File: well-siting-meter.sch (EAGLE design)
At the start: 46 parts, among them J2 7805, T1 MOSFET-NCHANNELFQP30N06L, U1 LCD-16X2NOHOLES, U2 ARDUINO_PRO_MINI, U3 EC2, U4 EC2, U5 AD623, U6 AD623

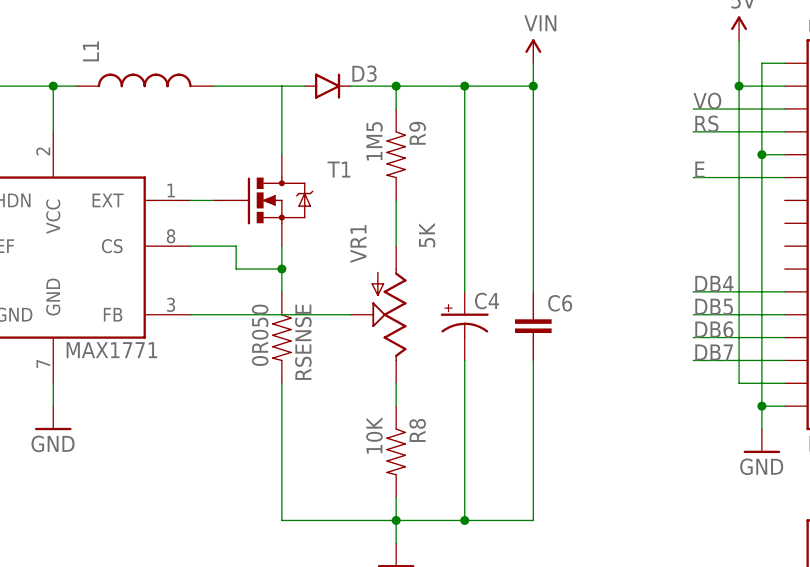
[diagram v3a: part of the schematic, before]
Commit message: adding part numbers
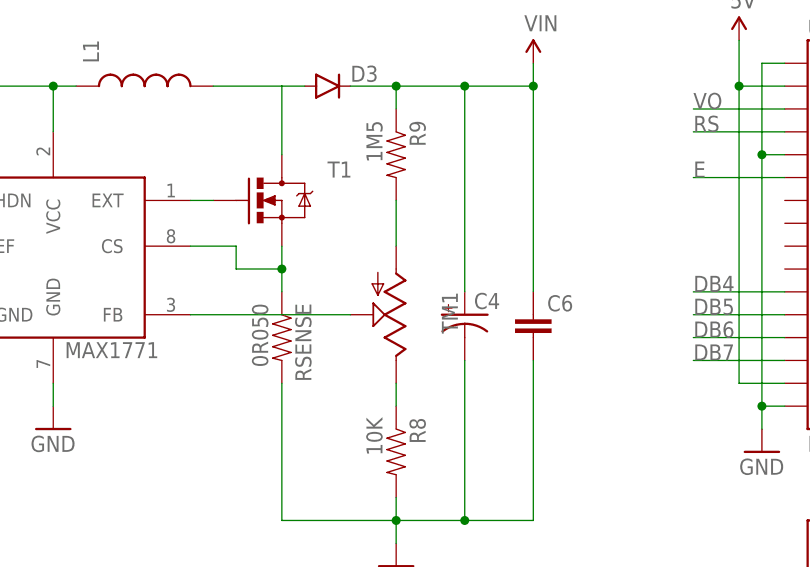
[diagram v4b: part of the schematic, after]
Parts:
- removed VR1: 5K, SparkFun-Electromechanical:POTTRIM
- added TM1: (no value), adafruit:TRIM3386
- D3: PN (none) -> EGP20FCT-ND
- T1: PN (none) -> FDP33N25-ND
- U$1: PN (none) -> MAX1771CPA+-ND
- U1: PN (none) -> 1528-1502-ND
- U2: PN (none) -> 1568-1055-ND
- U3, U4: PN (none) -> 399-11029-5-ND
- U5, U6: PN (none) -> AD623ANZ-ND
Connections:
- net N$15: now also TM1.S; no longer VR1.S
- net N$6: now also TM1.A; no longer VR1.A
- net N$8: now also TM1.E; no longer VR1.E
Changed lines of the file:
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@@
 <layer number="230" name="230bmp" color="7" fill="1" visible="yes" active="yes"/>
 <layer number="231" name="231bmp" color="7" fill="1" visible="yes" active="yes"/>
+<layer number="232" name="Eagle3D_PG2" color="7" fill="1" visible="no" active="no"/>
+<layer number="233" name="Eagle3D_PG3" color="7" fill="1" visible="no" active="no"/>
 <layer number="248" name="Housing" color="7" fill="1" visible="yes" active="yes"/>
 <layer number="249" name="Edge" color="7" fill="1" visible="yes" active="yes"/>
@@
 </classes>
 <parts>
-<part name="U3" library="ec2" deviceset="EC2" device=""/>
-<part name="U4" library="ec2" deviceset="EC2" device=""/>
-<part name="U2" library="SparkFun-Boards" deviceset="ARDUINO_PRO_MINI" device=""/>
-<part name="U5" library="ad623" deviceset="AD623" device=""/>
-<part name="U6" library="ad623" deviceset="AD623" device=""/>
+<part name="U3" library="ec2" deviceset="EC2" device="">
+<attribute name="PN" value="399-11029-5-ND"/>
+</part>
+<part name="U4" library="ec2" deviceset="EC2" device="">
+<attribute name="PN" value="399-11029-5-ND"/>
+</part>
+<part name="U2" library="SparkFun-Boards" deviceset="ARDUINO_PRO_MINI" device="">
+<attribute name="PN" value="1568-1055-ND"/>
+</part>
+<part name="U5" library="ad623" deviceset="AD623" device="">
+<attribute name="PN" value="AD623ANZ-ND"/>
+</part>
+<part name="U6" library="ad623" deviceset="AD623" device="">
+<attribute name="PN" value="AD623ANZ-ND"/>
+</part>
 <part name="Q1" library="SparkFun-DiscreteSemi" deviceset="TRANSISTOR_NPN" device="P2N2222A"/>
 <part name="Q2" library="SparkFun-DiscreteSemi" deviceset="TRANSISTOR_NPN" device="P2N2222A"/>
@@
 <part name="SUPPLY8" library="SparkFun-Aesthetics" deviceset="V_BATT" device=""/>
 <part name="GND8" library="SparkFun-Aesthetics" deviceset="GND" device=""/>
-<part name="U1" library="SparkFun-Displays" deviceset="LCD-16X2" device="NOHOLES" value="LCD-16X2NOHOLES"/>
+<part name="U1" library="SparkFun-Displays" deviceset="LCD-16X2" device="NOHOLES" value="LCD-16X2NOHOLES">
+<attribute name="PN" value="1528-1502-ND"/>
+</part>
 <part name="GND11" library="SparkFun-Aesthetics" deviceset="GND" device=""/>
 <part name="SUPPLY11" library="SparkFun-Aesthetics" deviceset="5V" device=""/>
@@
 <part name="C2" library="SparkFun-Passives" deviceset="CAP" device="PTH"/>
 <part name="C3" library="SparkFun-Passives" deviceset="CAP" device="PTH"/>
-<part name="T1" library="SparkFun-DiscreteSemi" deviceset="MOSFET-NCHANNEL" device="FQP30N06L"/>
-<part name="D3" library="SparkFun-DiscreteSemi" deviceset="DIODE" device="PTH"/>
+<part name="T1" library="SparkFun-DiscreteSemi" deviceset="MOSFET-NCHANNEL" device="FQP30N06L">
+<attribute name="PN" value="FDP33N25-ND"/>
+</part>
+<part name="D3" library="SparkFun-DiscreteSemi" deviceset="DIODE" device="PTH">
+<attribute name="PN" value="EGP20FCT-ND"/>
+</part>
 <part name="RSENSE" library="SparkFun-Passives" deviceset="RESISTOR" device="PTH-1/4W" value="0R050"/>
-<part name="VR1" library="SparkFun-Electromechanical" deviceset="POT" device="TRIM" value="5K"/>
 <part name="R8" library="SparkFun-Passives" deviceset="RESISTOR" device="PTH-1/4W" value="10K"/>
 <part name="R9" library="SparkFun-Passives" deviceset="RESISTOR" device="PTH-1/4W" value="1M5"/>
@@
 <part name="C4" library="SparkFun-Passives" deviceset="CAP_POL" device="PTH1"/>
 <part name="GND1" library="SparkFun-Aesthetics" deviceset="GND" device=""/>
-<part name="U$1" library="max1771" deviceset="MAX1771" device=""/>
+<part name="U$1" library="max1771" deviceset="MAX1771" device="">
+<attribute name="PN" value="MAX1771CPA+-ND"/>
+</part>
 <part name="R10" library="SparkFun-Passives" deviceset="RESISTOR" device="PTH-1/4W" value="1.02K"/>
 <part name="R11" library="SparkFun-Passives" deviceset="RESISTOR" device="PTH-1/4W" value="1.02K"/>
@@
 <part name="GND14" library="SparkFun-Aesthetics" deviceset="GND" device=""/>
 <part name="GND15" library="SparkFun-Aesthetics" deviceset="GND" device=""/>
+<part name="TM1" library="adafruit" deviceset="TRIM" device="3386"/>
 </parts>
 <sheets>
@@
 </plain>
 <instances>
-<instance part="U3" gate="G$1" x="124.46" y="154.94"/>
-<instance part="U4" gate="G$1" x="193.04" y="154.94"/>
-<instance part="U2" gate="G$1" x="144.78" y="119.38"/>
-<instance part="U5" gate="G$1" x="198.12" y="121.92"/>
-<instance part="U6" gate="G$1" x="198.12" y="81.28"/>
+<instance part="U3" gate="G$1" x="124.46" y="154.94">
+<attribute name="PN" x="124.46" y="154.94" size="1.778" layer="96" display="off"/>
+</instance>
+<instance part="U4" gate="G$1" x="193.04" y="154.94">
+<attribute name="PN" x="193.04" y="154.94" size="1.778" layer="96" display="off"/>
+</instance>
+<instance part="U2" gate="G$1" x="144.78" y="119.38">
+<attribute name="PN" x="144.78" y="119.38" size="1.778" layer="96" display="off"/>
+</instance>
+<instance part="U5" gate="G$1" x="198.12" y="121.92">
+<attribute name="PN" x="198.12" y="121.92" size="1.778" layer="96" display="off"/>
+</instance>
+<instance part="U6" gate="G$1" x="198.12" y="81.28">
+<attribute name="PN" x="198.12" y="81.28" size="1.778" layer="96" display="off"/>
+</instance>
 <instance part="Q1" gate="G$1" x="99.06" y="157.48"/>
 <instance part="Q2" gate="G$1" x="167.64" y="157.48"/>
@@
 <instance part="SUPPLY8" gate="G$1" x="25.4" y="86.36"/>
 <instance part="GND8" gate="1" x="25.4" y="48.26"/>
-<instance part="U1" gate="G$1" x="154.94" y="66.04"/>
+<instance part="U1" gate="G$1" x="154.94" y="66.04">
+<attribute name="PN" x="154.94" y="66.04" size="1.778" layer="96" display="off"/>
+</instance>
 <instance part="GND11" gate="1" x="142.24" y="43.18"/>
 <instance part="SUPPLY11" gate="G$1" x="139.7" y="88.9"/>
@@
 <instance part="T1" gate="G$1" x="88.9" y="71.12" smashed="yes">
 <attribute name="NAME" x="93.98" y="73.66" size="1.778" layer="95"/>
-</instance>
-<instance part="D3" gate="G$1" x="93.98" y="83.82"/>
+<attribute name="PN" x="88.9" y="71.12" size="1.778" layer="96" display="off"/>
+</instance>
+<instance part="D3" gate="G$1" x="93.98" y="83.82">
+<attribute name="PN" x="93.98" y="83.82" size="1.778" layer="96" display="off"/>
+</instance>
 <instance part="RSENSE" gate="G$1" x="88.9" y="55.88" rot="R270"/>
-<instance part="VR1" gate="G$1" x="101.6" y="58.42" rot="R180"/>
 <instance part="R8" gate="G$1" x="101.6" y="43.18" rot="R270"/>
 <instance part="R9" gate="G$1" x="101.6" y="76.2" rot="R270"/>
@@
 <instance part="C4" gate="G$1" x="109.22" y="58.42"/>
 <instance part="GND1" gate="1" x="63.5" y="45.72"/>
-<instance part="U$1" gate="G$1" x="63.5" y="63.5"/>
+<instance part="U$1" gate="G$1" x="63.5" y="63.5">
+<attribute name="PN" x="63.5" y="63.5" size="1.778" layer="96" display="off"/>
+</instance>
 <instance part="R10" gate="G$1" x="215.9" y="121.92"/>
 <instance part="R11" gate="G$1" x="215.9" y="81.28"/>
@@
 <instance part="GND14" gate="1" x="223.52" y="106.68"/>
 <instance part="GND15" gate="1" x="223.52" y="66.04"/>
+<instance part="TM1" gate="G$1" x="101.6" y="58.42" rot="R180"/>
 </instances>
 <busses>
@@
 <segment>
 <pinref part="R9" gate="G$1" pin="2"/>
-<pinref part="VR1" gate="G$1" pin="A"/>
 <wire x1="101.6" y1="71.12" x2="101.6" y2="66.04" width="0.1524" layer="91"/>
+<pinref part="TM1" gate="G$1" pin="A"/>
 </segment>
 </net>
 <net name="N$8" class="0">
 <segment>
-<pinref part="VR1" gate="G$1" pin="E"/>
 <pinref part="R8" gate="G$1" pin="1"/>
 <wire x1="101.6" y1="50.8" x2="101.6" y2="48.26" width="0.1524" layer="91"/>
+<pinref part="TM1" gate="G$1" pin="E"/>
 </segment>
 </net>
 <net name="N$15" class="0">
 <segment>
-<pinref part="VR1" gate="G$1" pin="S"/>
 <wire x1="78.74" y1="58.42" x2="96.52" y2="58.42" width="0.1524" layer="91"/>
 <pinref part="U$1" gate="G$1" pin="FB"/>
-</segment>
-</net>
+<pinref part="TM1" gate="G$1" pin="S"/>
+</segment>
+</net>

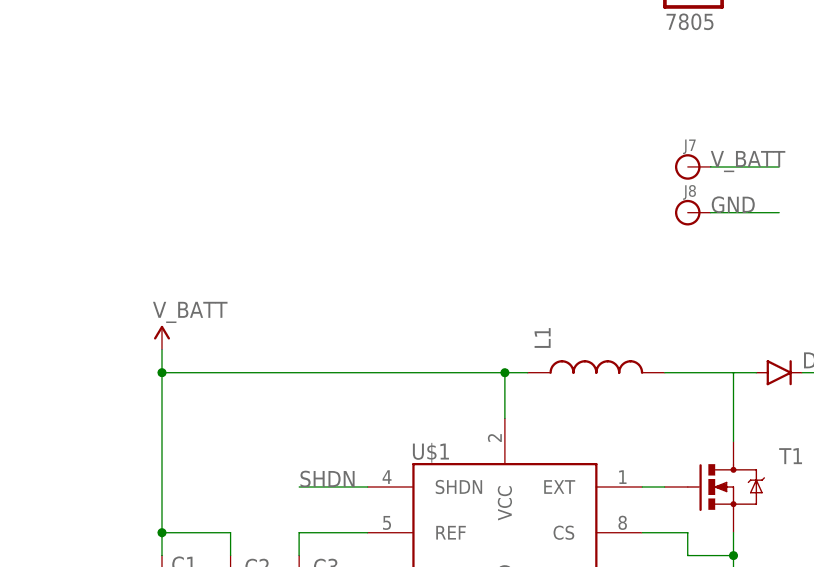
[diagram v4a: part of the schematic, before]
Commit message: updated inductor, adding part numbers
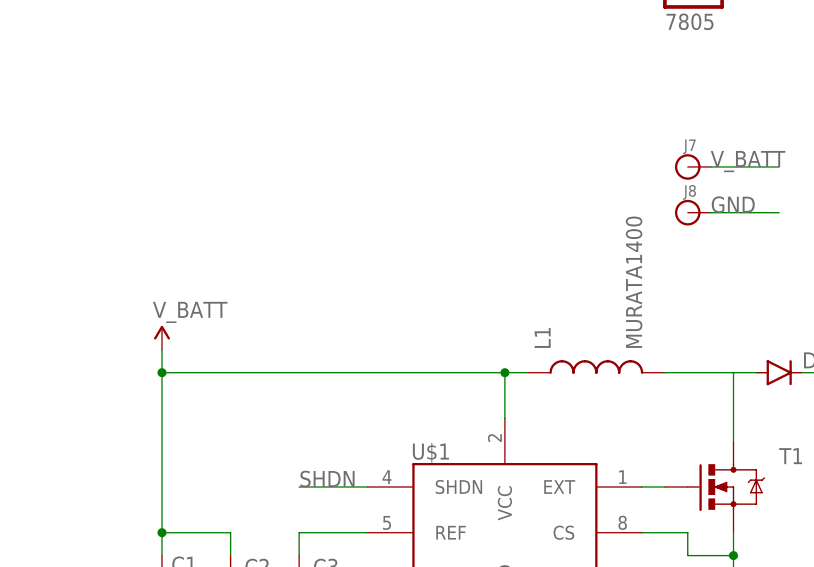
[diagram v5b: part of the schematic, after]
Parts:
- D1, D2: PN (none) -> 1N4001FSCT-ND
- L1: value (none) -> MURATA1400; device SparkFun-Passives:INDUCTORRLB0912 -> murata1400:MURATA1400; PN (none) -> 811-2633-ND
- Q1, Q2: PN (none) -> PN2222AFS-ND
- RSENSE: device SparkFun-Passives:RESISTORPTH-1/4W -> SparkFun-Passives:RESISTORPTH-1W
- S1, S2: PN (none) -> SW406-ND

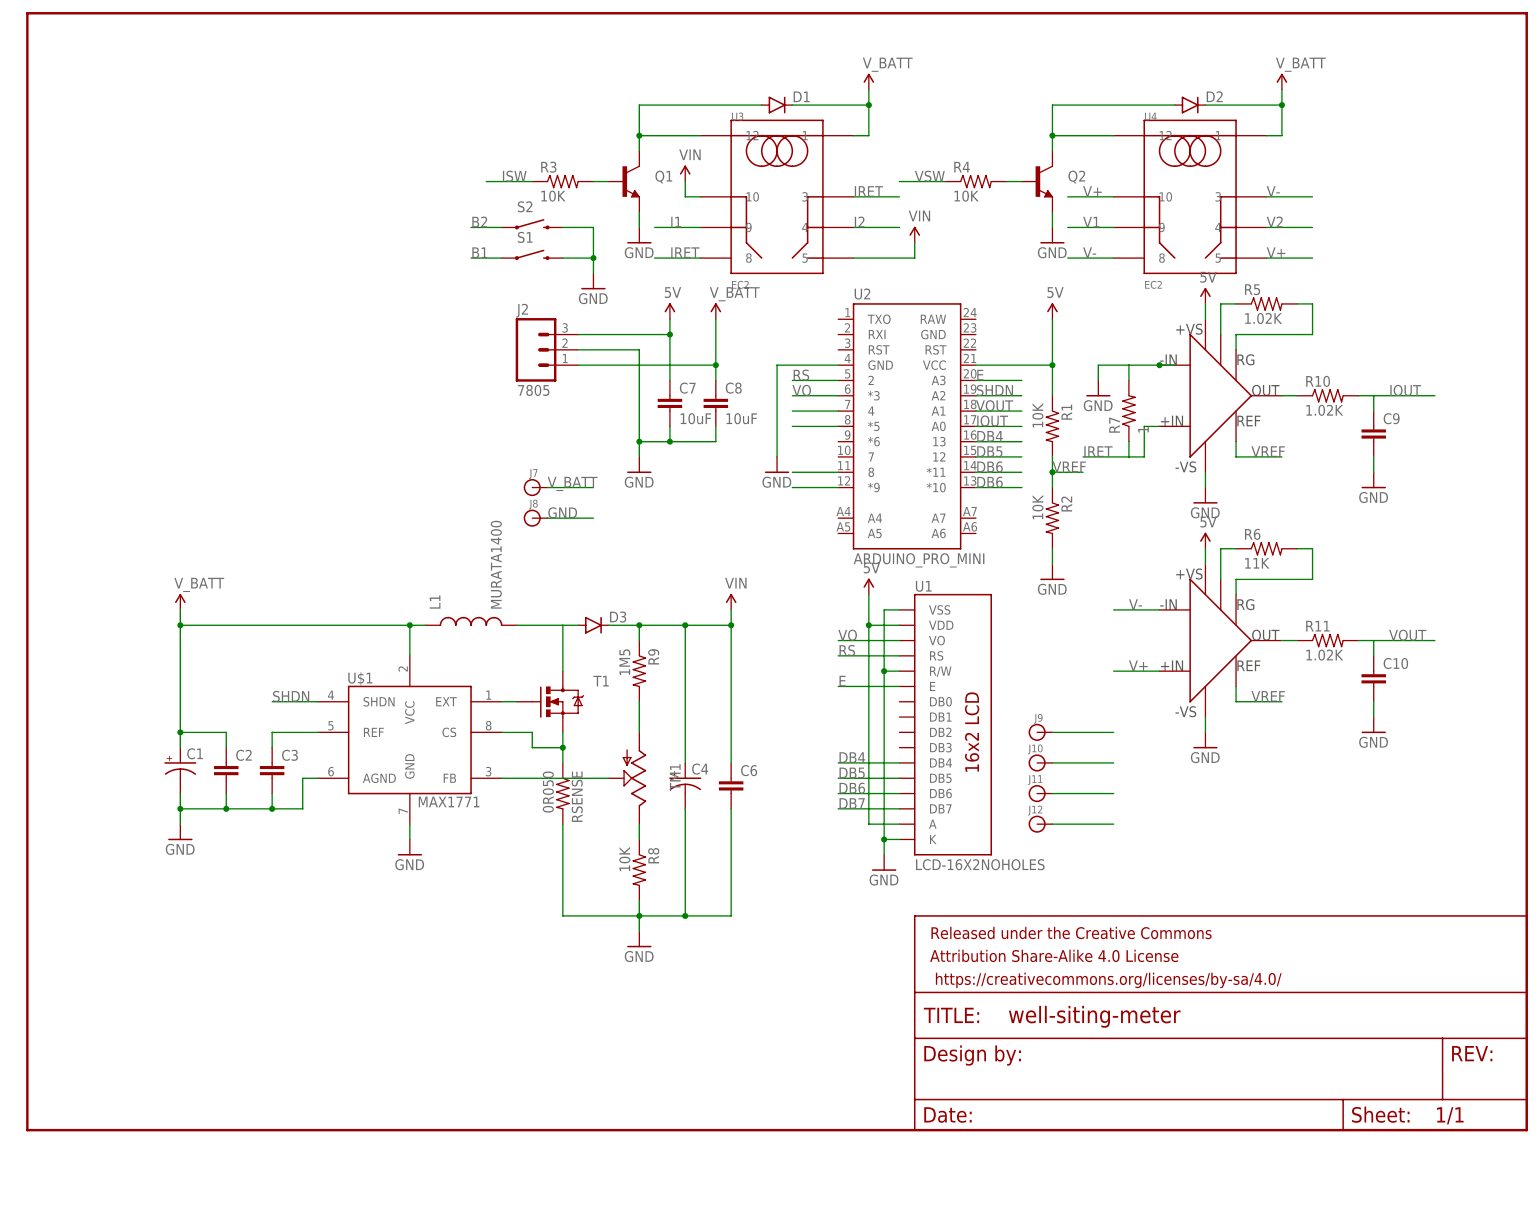
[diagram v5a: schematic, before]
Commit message: fixed board outline, added remaining part numbers
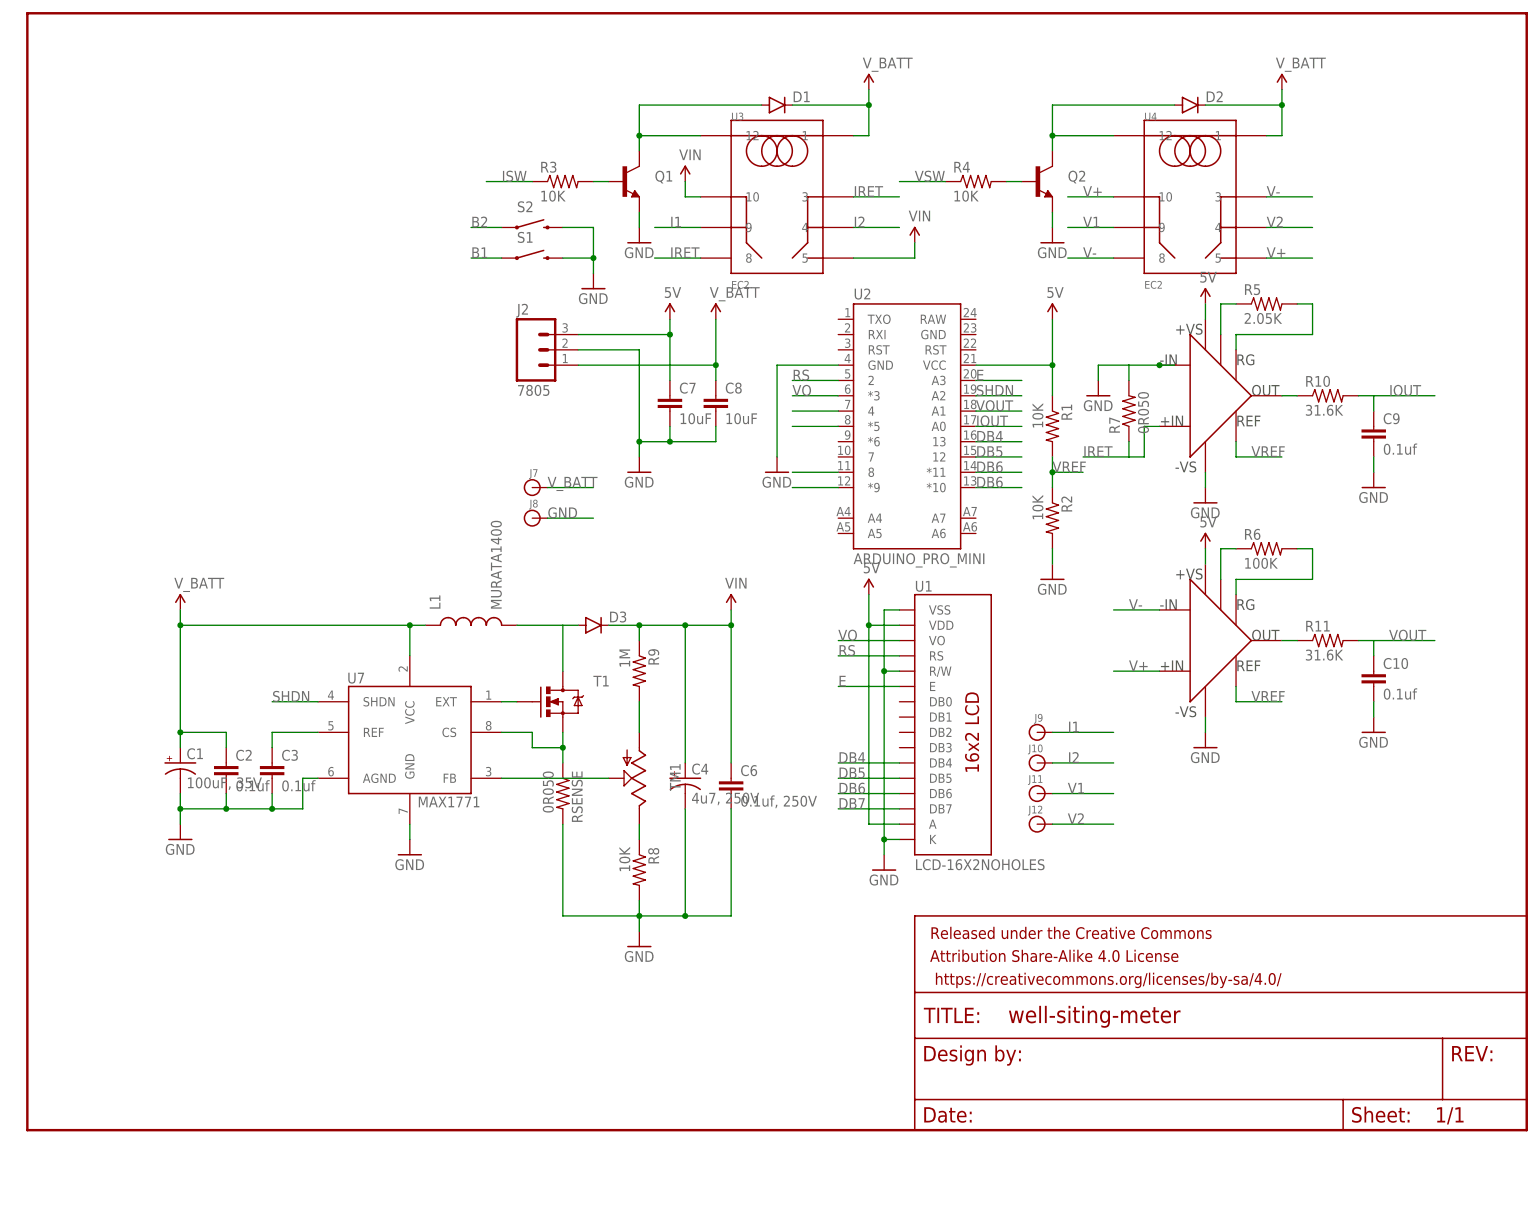
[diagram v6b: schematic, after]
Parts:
- C1: value (none) -> 100uF, 35V; PN (none) -> 1572-1306-ND
- C10, C2, C3, C9: value (none) -> 0.1uf; PN (none) -> BC2665CT-ND
- C4: value (none) -> 4u7, 250V; PN (none) -> 399-6091-ND
- C6: value (none) -> 0.1uf, 250V; PN (none) -> 445-173449-1-ND
- C7, C8: PN 490-7202-1-ND -> 445-173437-1-ND
- D1, D2: PN 1N4001FSCT-ND -> 1N4001-TPMSCT-ND
- J10, J12, J8: PN (none) -> 1568-1665-ND
- J11, J7, J9: PN (none) -> 1568-1664-ND
- R1, R2, R3, R4, R8: PN (none) -> 10.0KXBK-ND
- R10, R11: value 1.02K -> 31.6K; PN (none) -> 31.6KXBK-ND
- R5: value 1.02K -> 2.05K; PN (none) -> 2.05KXBK-ND
- R6: value 11K -> 100K; PN (none) -> 100KXBK-ND
- R7: value 1 -> 0R050; PN (none) -> 696-1731-ND
- R9: value 1M5 -> 1M; PN (none) -> 1.00MXBK-ND
- RSENSE: PN (none) -> 696-1731-ND
- renumbered U$1 to U7
